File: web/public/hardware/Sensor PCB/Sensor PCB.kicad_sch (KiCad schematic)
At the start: 32 parts, among them J1 Conn_01x08_Pin, J2 Conn_01x08_Pin, J3 Conn_01x02_Pin, J4 Conn_01x02_Pin, U1 DRV5033FAQDBZR, U2 DRV5033FAQDBZR, U3 DRV5033FAQDBZR, U4 DRV5033FAQDBZR, U5 CD74HCT11, U6 CD74HCT11

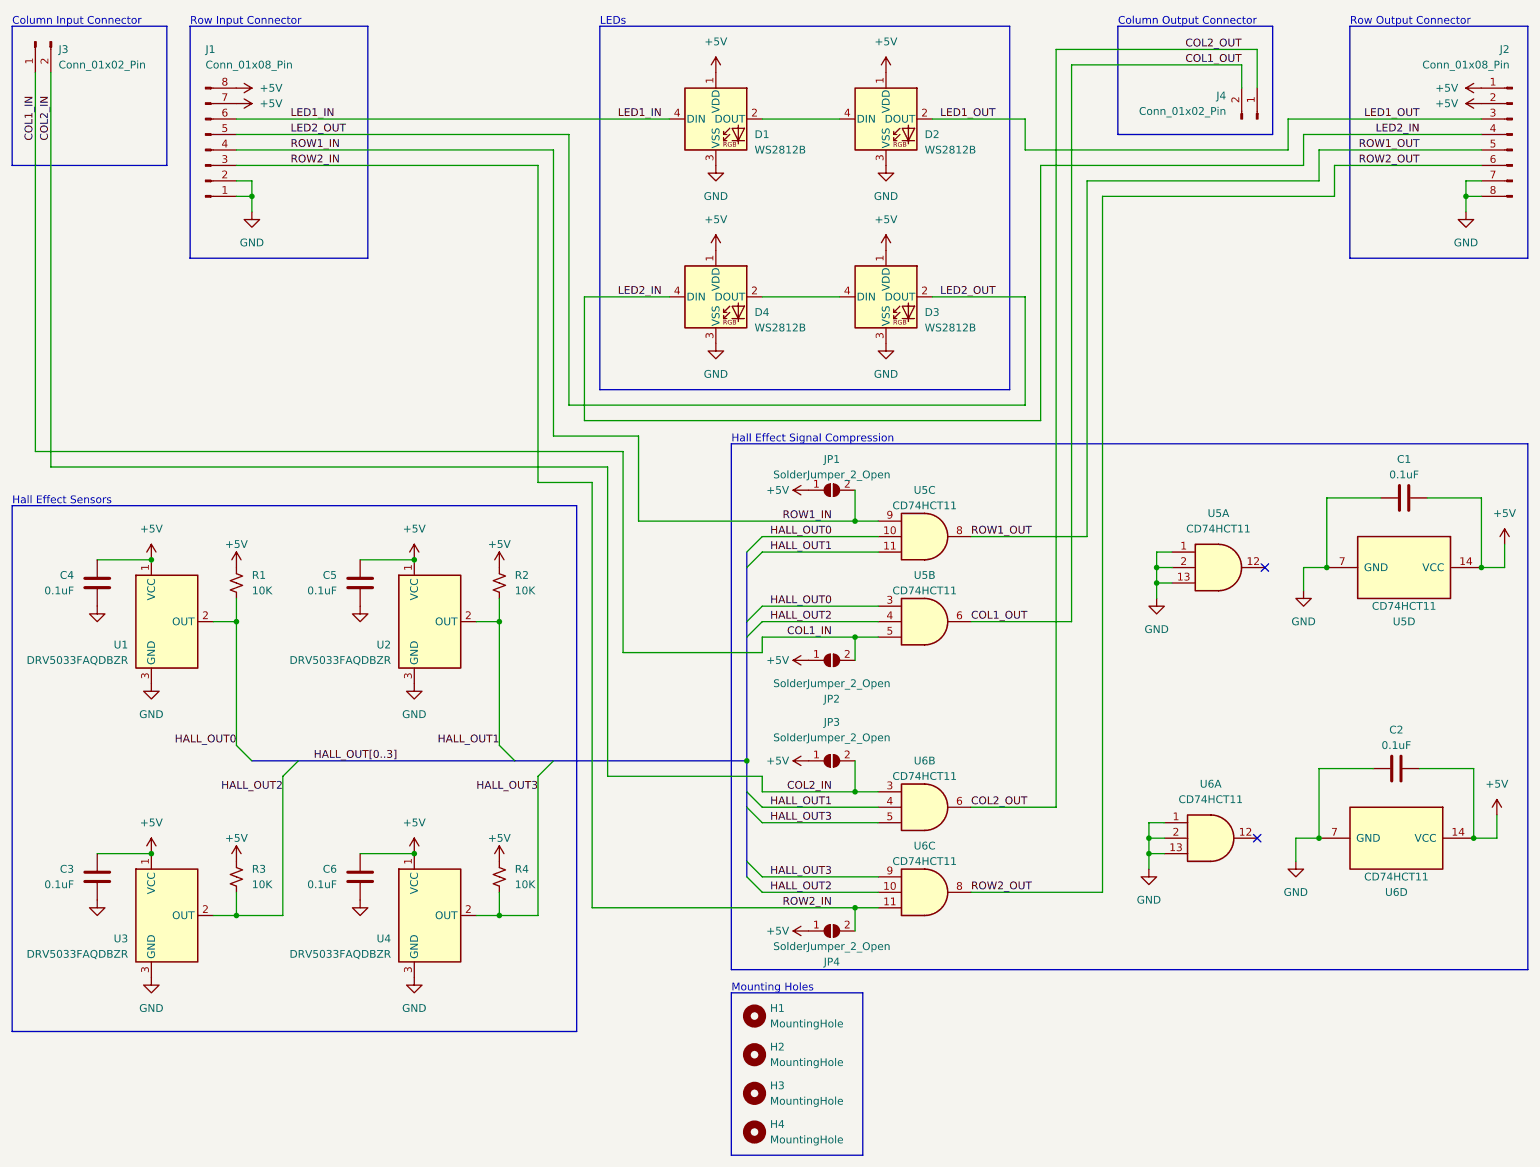
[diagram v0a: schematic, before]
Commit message: Updated based on Ben's feedback
Removed wires between blocks, instead relying on them being connected based on net names (pained me to do this)
Fixed D3/D4 so they match the PCB layout
Renamed minor components that were previously unnamed
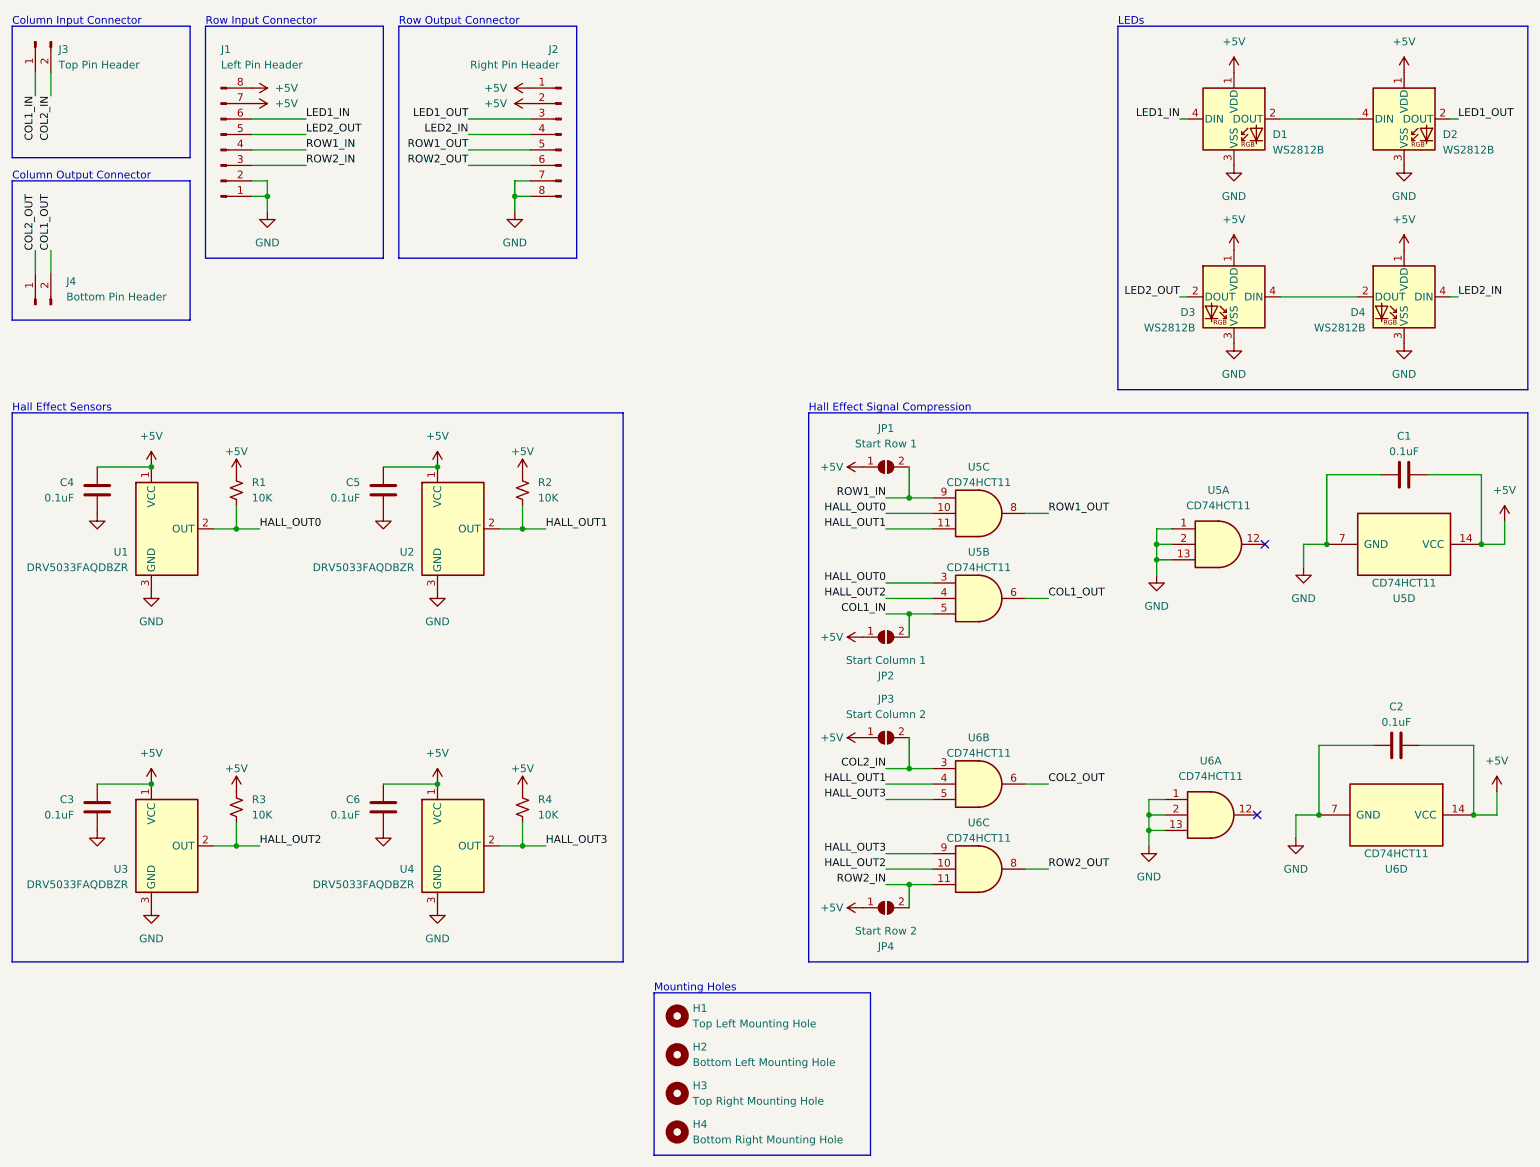
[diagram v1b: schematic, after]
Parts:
- H1: value MountingHole -> Top Left Mounting Hole
- H2: value MountingHole -> Bottom Left Mounting Hole
- H3: value MountingHole -> Top Right Mounting Hole
- H4: value MountingHole -> Bottom Right Mounting Hole
- J1: value Conn_01x08_Pin -> Left Pin Header
- J2: value Conn_01x08_Pin -> Right Pin Header
- J3: value Conn_01x02_Pin -> Top Pin Header
- J4: value Conn_01x02_Pin -> Bottom Pin Header
- JP1: value SolderJumper_2_Open -> Start Row 1
- JP2: value SolderJumper_2_Open -> Start Column 1
- JP3: value SolderJumper_2_Open -> Start Column 2
- JP4: value SolderJumper_2_Open -> Start Row 2
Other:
- moved on the sheet: C1, C2, C3, C4, C5, C6, D1, D2, D3, D4, H1, H2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

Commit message: Add JLCPCB assembly files
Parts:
- C1, C2, C3, C4, C5, C6: JLCPCB Part # (none) -> C49678
- D2, D3, D4: JLCPCB Part # (none) -> C4154882
- J1, J2: JLCPCB Part # (none) -> C492416; JLCPCB Position Offset (none) -> -8.89,0; JLCPCB Rotation Offset (none) -> 90
- J3, J4: JLCPCB Part # (none) -> C492410; JLCPCB Position Offset (none) -> -1.27,0; JLCPCB Rotation Offset (none) -> 90
- R1, R2, R3, R4: JLCPCB Part # (none) -> C100047
- U1, U2, U3, U4: JLCPCB Part # (none) -> C2655029; JLCPCB Rotation Offset (none) -> 180
- U5, U6: JLCPCB Part # (none) -> C7643; JLCPCB Rotation Offset (none) -> -90
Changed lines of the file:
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@@
   (title_block
     (title "Sensor PCB")
-    (date "2023-09-19")
+    (date "2023-10-18")
     (rev "A")
     (company "ECE 477")
@@
     )
     (property "Datasheet" "http://www.ti.com/lit/gpn/sn74LS11" (at 243.84 100.33 0)
+      (effects (font (size 1.27 1.27)) hide)
+    )
+    (property "JLCPCB Part #" "C7643" (at 243.84 100.33 0)
+      (effects (font (size 1.27 1.27)) hide)
+    )
+    (property "JLCPCB Rotation Offset" "-90" (at 243.84 100.33 0)
       (effects (font (size 1.27 1.27)) hide)
     )
@@
       (effects (font (size 1.27 1.27)) hide)
     )
+    (property "JLCPCB Part #" "C7643" (at 173.99 139.7 0)
+      (effects (font (size 1.27 1.27)) hide)
+    )
+    (property "JLCPCB Rotation Offset" "-90" (at 173.99 139.7 0)
+      (effects (font (size 1.27 1.27)) hide)
+    )
     (pin "1")
     (pin "12")
@@
       (effects (font (size 1.27 1.27)) hide)
     )
+    (property "JLCPCB Part #" "C100047" (at 99.06 143.51 0)
+      (effects (font (size 1.27 1.27)) hide)
+    )
     (pin "1")
     (pin "2")
@@
     )
     (property "Datasheet" "http://www.ti.com/lit/gpn/sn74LS11" (at 173.99 109.22 0)
+      (effects (font (size 1.27 1.27)) hide)
+    )
+    (property "JLCPCB Part #" "C7643" (at 173.99 109.22 0)
+      (effects (font (size 1.27 1.27)) hide)
+    )
+    (property "JLCPCB Rotation Offset" "-90" (at 173.99 109.22 0)
       (effects (font (size 1.27 1.27)) hide)
     )
@@
       (effects (font (size 1.27 1.27)) hide)
     )
+    (property "JLCPCB Part #" "C2655029" (at 87.63 97.79 0)
+      (effects (font (size 1.27 1.27)) hide)
+    )
+    (property "JLCPCB Rotation Offset" "180" (at 87.63 97.79 0)
+      (effects (font (size 1.27 1.27)) hide)
+    )
     (pin "1")
     (pin "2")
@@
     )
     (property "Datasheet" "~" (at 49.53 35.56 0)
+      (effects (font (size 1.27 1.27)) hide)
+    )
+    (property "JLCPCB Part #" "C492416" (at 49.53 35.56 0)
+      (effects (font (size 1.27 1.27)) hide)
+    )
+    (property "JLCPCB Rotation Offset" "90" (at 49.53 35.56 0)
+      (effects (font (size 1.27 1.27)) hide)
+    )
+    (property "JLCPCB Position Offset" "-8.89,0" (at 49.53 35.56 0)
       (effects (font (size 1.27 1.27)) hide)
     )
@@
       (effects (font (size 1.27 1.27)) hide)
     )
+    (property "JLCPCB Part #" "C49678" (at 243.84 88.9 90)
+      (effects (font (size 1.27 1.27)) hide)
+    )
     (pin "1")
     (pin "2")
@@
     )
     (property "Datasheet" "~" (at 52.07 91.44 0)
+      (effects (font (size 1.27 1.27)) hide)
+    )
+    (property "JLCPCB Part #" "C100047" (at 52.07 91.44 0)
       (effects (font (size 1.27 1.27)) hide)
     )
@@
       (effects (font (size 1.27 1.27)) hide)
     )
+    (property "JLCPCB Part #" "C492410" (at 19.05 60.96 90)
+      (effects (font (size 1.27 1.27)) hide)
+    )
+    (property "JLCPCB Rotation Offset" "90" (at 19.05 60.96 90)
+      (effects (font (size 1.27 1.27)) hide)
+    )
+    (property "JLCPCB Position Offset" "-1.27,0" (at 19.05 60.96 90)
+      (effects (font (size 1.27 1.27)) hide)
+    )
     (pin "1")
     (pin "2")
@@
       (effects (font (size 1.27 1.27)) (justify left top) hide)
     )
+    (property "JLCPCB Part #" "C4154882" (at 243.84 30.48 0)
+      (effects (font (size 1.27 1.27)) hide)
+    )
     (pin "1")
     (pin "2")
@@
     )
     (property "Datasheet" "http://www.ti.com/lit/gpn/sn74LS11" (at 242.57 144.78 0)
+      (effects (font (size 1.27 1.27)) hide)
+    )
+    (property "JLCPCB Part #" "C7643" (at 242.57 144.78 0)
+      (effects (font (size 1.27 1.27)) hide)
+    )
+    (property "JLCPCB Rotation Offset" "-90" (at 242.57 144.78 0)
       (effects (font (size 1.27 1.27)) hide)
     )
@@
       (effects (font (size 1.27 1.27)) hide)
     )
+    (property "JLCPCB Part #" "C2655029" (at 87.63 149.86 0)
+      (effects (font (size 1.27 1.27)) hide)
+    )
+    (property "JLCPCB Rotation Offset" "180" (at 87.63 149.86 0)
+      (effects (font (size 1.27 1.27)) hide)
+    )
     (pin "1")
     (pin "2")
@@
     )
     (property "Datasheet" "~" (at 29.21 91.44 0)
+      (effects (font (size 1.27 1.27)) hide)
+    )
+    (property "JLCPCB Part #" "C49678" (at 29.21 91.44 0)
       (effects (font (size 1.27 1.27)) hide)
     )
@@
       (effects (font (size 1.27 1.27)) hide)
     )
+    (property "JLCPCB Part #" "C49678" (at 29.21 143.51 0)
+      (effects (font (size 1.27 1.27)) hide)
+    )
     (pin "1")
     (pin "2")
@@
     )
     (property "Datasheet" "http://www.ti.com/lit/gpn/sn74LS11" (at 213.36 100.33 0)
+      (effects (font (size 1.27 1.27)) hide)
+    )
+    (property "JLCPCB Part #" "C7643" (at 213.36 100.33 0)
+      (effects (font (size 1.27 1.27)) hide)
+    )
+    (property "JLCPCB Rotation Offset" "-90" (at 213.36 100.33 0)
       (effects (font (size 1.27 1.27)) hide)
     )
@@
       (effects (font (size 1.27 1.27)) hide)
     )
+    (property "JLCPCB Part #" "C492416" (at 105.41 33.02 0)
+      (effects (font (size 1.27 1.27)) hide)
+    )
+    (property "JLCPCB Rotation Offset" "90" (at 105.41 33.02 0)
+      (effects (font (size 1.27 1.27)) hide)
+    )
+    (property "JLCPCB Position Offset" "-8.89,0" (at 105.41 33.02 0)
+      (effects (font (size 1.27 1.27)) hide)
+    )
     (pin "1")
     (pin "2")
@@
     )
     (property "Datasheet" "http://www.ti.com/lit/gpn/sn74LS11" (at 173.99 153.67 0)
+      (effects (font (size 1.27 1.27)) hide)
+    )
+    (property "JLCPCB Part #" "C7643" (at 173.99 153.67 0)
+      (effects (font (size 1.27 1.27)) hide)
+    )
+    (property "JLCPCB Rotation Offset" "-90" (at 173.99 153.67 0)
       (effects (font (size 1.27 1.27)) hide)
     )
@@
       (effects (font (size 1.27 1.27)) hide)
     )
+    (property "JLCPCB Part #" "C100047" (at 99.06 91.44 0)
+      (effects (font (size 1.27 1.27)) hide)
+    )
     (pin "1")
     (pin "2")
@@
       (effects (font (size 1.27 1.27)) hide)
     )
+    (property "JLCPCB Part #" "C2655029" (at 40.64 149.86 0)
+      (effects (font (size 1.27 1.27)) hide)
+    )
+    (property "JLCPCB Rotation Offset" "180" (at 40.64 149.86 0)
+      (effects (font (size 1.27 1.27)) hide)
+    )
     (pin "1")
     (pin "2")
@@
       (effects (font (size 1.27 1.27)) (justify left top) hide)
     )
+    (property "JLCPCB Part #" "C4154882" (at 215.9 59.69 0)
+      (effects (font (size 1.27 1.27)) hide)
+    )
     (pin "1")
     (pin "2")
@@
       (effects (font (size 1.27 1.27)) hide)
     )
+    (property "JLCPCB Part #" "C100047" (at 52.07 143.51 0)
+      (effects (font (size 1.27 1.27)) hide)
+    )
     (pin "1")
     (pin "2")
@@
       (effects (font (size 1.27 1.27)) hide)
     )
+    (property "JLCPCB Part #" "C49678" (at 242.57 133.35 90)
+      (effects (font (size 1.27 1.27)) hide)
+    )
     (pin "1")
     (pin "2")
@@
     )
     (property "Datasheet" "http://www.ti.com/lit/gpn/sn74LS11" (at 212.09 144.78 0)
+      (effects (font (size 1.27 1.27)) hide)
+    )
+    (property "JLCPCB Part #" "C7643" (at 212.09 144.78 0)
+      (effects (font (size 1.27 1.27)) hide)
+    )
+    (property "JLCPCB Rotation Offset" "-90" (at 212.09 144.78 0)
       (effects (font (size 1.27 1.27)) hide)
     )
@@
       (effects (font (size 1.27 1.27)) hide)
     )
+    (property "JLCPCB Part #" "C49678" (at 76.2 91.44 0)
+      (effects (font (size 1.27 1.27)) hide)
+    )
     (pin "1")
     (pin "2")
@@
     )
     (property "Datasheet" "http://www.ti.com/lit/gpn/sn74LS11" (at 173.99 95.25 0)
+      (effects (font (size 1.27 1.27)) hide)
+    )
+    (property "JLCPCB Part #" "C7643" (at 173.99 95.25 0)
+      (effects (font (size 1.27 1.27)) hide)
+    )
+    (property "JLCPCB Rotation Offset" "-90" (at 173.99 95.25 0)
       (effects (font (size 1.27 1.27)) hide)
     )
@@
       (effects (font (size 1.27 1.27)) hide)
     )
+    (property "JLCPCB Part #" "C2655029" (at 40.64 97.79 0)
+      (effects (font (size 1.27 1.27)) hide)
+    )
+    (property "JLCPCB Rotation Offset" "180" (at 40.64 97.79 0)
+      (effects (font (size 1.27 1.27)) hide)
+    )
     (pin "1")
     (pin "2")
@@
     )
     (property "Datasheet" "~" (at 76.2 143.51 0)
+      (effects (font (size 1.27 1.27)) hide)
+    )
+    (property "JLCPCB Part #" "C49678" (at 76.2 143.51 0)
       (effects (font (size 1.27 1.27)) hide)
     )
@@
       (effects (font (size 1.27 1.27)) (justify left top) hide)
     )
+    (property "JLCPCB Part #" "C4154882" (at 243.84 59.69 0)
+      (effects (font (size 1.27 1.27)) hide)
+    )
     (pin "1")
     (pin "2")
@@
       (effects (font (size 1.27 1.27)) hide)
     )
+    (property "JLCPCB Part #" "C492410" (at 19.05 17.78 90)
+      (effects (font (size 1.27 1.27)) hide)
+    )
+    (property "JLCPCB Rotation Offset" "90" (at 19.05 17.78 90)
+      (effects (font (size 1.27 1.27)) hide)
+    )
+    (property "JLCPCB Position Offset" "-1.27,0" (at 19.05 17.78 90)
+      (effects (font (size 1.27 1.27)) hide)
+    )

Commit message: I forgor one LED part number
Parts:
- D1: JLCPCB Part # (none) -> C4154882
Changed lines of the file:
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@@
       (effects (font (size 1.27 1.27)) (justify left top) hide)
+    )
+    (property "JLCPCB Part #" "C4154882" (at 215.9 30.48 0)
+      (effects (font (size 1.27 1.27)) hide)
     )
     (pin "1")
